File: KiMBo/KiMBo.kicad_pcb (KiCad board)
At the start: 6 copper layers, 187 x 127 mm, 217 parts, among them P1 TOOLHEAD0, P10 ADC, P11 Serial, P12 μUSB, P13 USB_Type_A, P14 μSD, P15 Ethernet, P16 JTAG, P17 LCD, P18 E_MOTOR, P2 TOOLHEAD1, P20 X0_MOTOR, P21 X1_MOTOR, P22 Y_MOTOR, P24 Z0_MOTOR, P27 BED_HEAT, P28 E_HEAT, P29 H_HEAT, P3 DOCK0, P30 DOCK0_HEAT, P31 DOCK1_HEAT, P32 E_FAN, P33 H_FAN, P34 CASE_FAN, P35 PWM, P36 PWR_Input, P4 DOCK1, P5 X1, P6 Y1, P7 Z1, P8 ENC, P9 BED_THERM, U1 OSD3358, U11 74HC595, U12 74HC595, U14 TMC2130, U15 TMC2130, U16 TMC2130, U20 TMC2130, U21 TMC2130, U5 EMMC**G-S100, U6 TPS2051B

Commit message: Complete stepper footprint association, move silkscreen, start DC fuse, polarity protection, and circuit
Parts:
- added C1: 100nF, Capacitors_SMD:C_0603, F.Cu at (409.4, 81.5)
- added C10: 470μF, KiMBo:c_elec_16x16.5, F.Cu at (499.8, 73.6)
- added C11: 220μF, KiMBo:c_elec_8x10.2, F.Cu at (515.2, 86.1)
- added C12: 22μF, Capacitors_SMD:C_0805, F.Cu at (93.5, 154.0)
- added C13: 22μF, Capacitors_SMD:C_0805, F.Cu at (93.5, 156.0)
- added C14: 100nF, Capacitors_SMD:C_0603, F.Cu at (494.3, 151.4)
- added C15: 2.2μF, Capacitors_SMD:C_0805, F.Cu at (469.4, 157.7)
- added C16: 100nF, Capacitors_SMD:C_0603, F.Cu at (488.4, 157.3)
- added C17: 100nF, Capacitors_SMD:C_0603, F.Cu at (484.0, 163.1)
- added C18: 2.2μF, Capacitors_SMD:C_0805, F.Cu at (464.6, 158.6)
- added C187: 100nF, Capacitors_SMD:C_0603, F.Cu at (551.6, 123.4)
- added C188: 4.7nF, Capacitors_SMD:C_0603, F.Cu at (403.4, 131.5)
- added C189: 4.7nF, Capacitors_SMD:C_0603, F.Cu at (410.0, 122.6)
- added C19: 100nF, Capacitors_SMD:C_0603, F.Cu at (477.6, 169.4)
- added C190: 4.7nF, Capacitors_SMD:C_0603, F.Cu at (389.0, 149.8)
- added C191: 4.7nF, Capacitors_SMD:C_0603, F.Cu at (408.0, 130.7)
- added C192: 4.7nF, Capacitors_SMD:C_0603, F.Cu at (402.9, 137.3)
- added C193: 4.7nF, Capacitors_SMD:C_0603, F.Cu at (436.8, 138.1)
- added C194: 4.7nF, Capacitors_SMD:C_0603, F.Cu at (461.5, 116.8)
- added C195: 4.7nF, Capacitors_SMD:C_0603, F.Cu at (447.3, 131.5)
- added C196: 47pF, Capacitors_SMD:C_0603, F.Cu at (515.9, 106.8)
- added C197: 47pF, Capacitors_SMD:C_0603, F.Cu at (498.5, 124.3)
- added C198: 47pF, Capacitors_SMD:C_0603, F.Cu at (510.7, 112.6)
- added C199: 47pF, Capacitors_SMD:C_0603, F.Cu at (502.9, 124.3)
- added C2: 100nF, Capacitors_SMD:C_0603, F.Cu at (402.9, 94.2)
- added C20: 2.2μF, Capacitors_SMD:C_0805, F.Cu at (461.1, 165.2)
- added C200: 47pF, Capacitors_SMD:C_0603, F.Cu at (515.1, 112.6)
- added C201: 47pF, Capacitors_SMD:C_0603, F.Cu at (520.3, 106.8)
- added C202: 47pF, Capacitors_SMD:C_0603, F.Cu at (503.8, 118.5)
- added C203: 47pF, Capacitors_SMD:C_0603, F.Cu at (512.6, 118.5)
- added C204: 47pF, Capacitors_SMD:C_0603, F.Cu at (520.5, 124.3)
- added C205: 47pF, Capacitors_SMD:C_0603, F.Cu at (516.1, 124.3)
- added C206: 47pF, Capacitors_SMD:C_0603, F.Cu at (517.0, 118.5)
- added C207: 47pF, Capacitors_SMD:C_0603, F.Cu at (511.7, 124.3)
- added C208: 47pF, Capacitors_SMD:C_0603, F.Cu at (519.5, 112.6)
- added C209: 47pF, Capacitors_SMD:C_0603, F.Cu at (507.3, 124.3)
- added C21: 4.7μF, Capacitors_SMD:C_0805, F.Cu at (476.1, 151.6)
- added C210: 47pF, Capacitors_SMD:C_0603, F.Cu at (511.5, 106.8)
- added C211: 47pF, Capacitors_SMD:C_0603, F.Cu at (508.2, 118.5)
- added C22: 100nF, Capacitors_SMD:C_0603, F.Cu at (478.8, 163.5)
- added C23: 100nF, Capacitors_SMD:C_0603, F.Cu at (483.2, 157.3)
- added C24: 220μF, Capacitors_Tantalum_SMD:TantalC_SizeD_EIA-7343_Reflow, F.Cu at (559.2, 70.6)
- added C25: 100nF, Capacitors_SMD:C_0603, F.Cu at (571.0, 81.2)
- added C26: 100nF, Capacitors_SMD:C_0603, F.Cu at (566.6, 75.3)
- added C27: 100nF, Capacitors_SMD:C_0603, F.Cu at (576.2, 80.9)
- added C28: 30pF, Capacitors_SMD:C_0603, F.Cu at (466.2, 86.7)
- added C29: 30pF, Capacitors_SMD:C_0603, F.Cu at (480.2, 75.0)
- added C3: 10nF, Capacitors_SMD:C_0603, F.Cu at (402.3, 100.0)
- added C30: 100nF, Capacitors_SMD:C_0603, F.Cu at (464.3, 92.6)
- added C31: 100nF, Capacitors_SMD:C_0603, F.Cu at (474.2, 80.9)
- added C32: 100nF, Capacitors_SMD:C_0603, F.Cu at (470.9, 86.7)
- added C33: 470pF, Capacitors_SMD:C_0603, F.Cu at (450.4, 80.9)
- added C34: 10μF, Capacitors_SMD:C_0805, F.Cu at (436.3, 90.6)
- added C35: 1μF, Capacitors_SMD:C_0603, F.Cu at (481.6, 69.2)
- added C36: DNP-15pF, Capacitors_SMD:C_0603, F.Cu at (429.9, 83.2)
- added C37: DNP-15pF, Capacitors_SMD:C_0603, F.Cu at (429.9, 89.0)
- added C38: DNP-15pF, Capacitors_SMD:C_0603, F.Cu at (443.6, 78.7)
- added C39: DNP-15pF, Capacitors_SMD:C_0603, F.Cu at (452.3, 69.2)
- added C4: 10nF, Capacitors_SMD:C_0603, F.Cu at (407.6, 93.2)
- added C40: 10μF, Capacitors_SMD:C_0603, F.Cu at (536.0, 162.7)
- added C41: 10μF, Capacitors_SMD:C_0603, F.Cu at (540.4, 156.9)
- added C42: 18pF, Capacitors_SMD:C_0603, F.Cu at (524.8, 141.1)
- added C43: 18pF, Capacitors_SMD:C_0603, F.Cu at (520.6, 141.1)
- added C44: 18pF, Capacitors_SMD:C_0603, F.Cu at (529.4, 135.2)
- added C45: 18pF, Capacitors_SMD:C_0603, F.Cu at (525.2, 135.2)
- added C46: 4.7μF, Capacitors_SMD:C_0603, F.Cu at (523.4, 162.7)
- added C47: 4.7μF, Capacitors_SMD:C_0603, F.Cu at (528.2, 162.7)
- added C48: 39nF, Capacitors_SMD:C_0603, F.Cu at (442.1, 161.8)
- added C49: 39nF, Capacitors_SMD:C_0603, F.Cu at (421.1, 181.7)
- added C5: 100nF, Capacitors_SMD:C_0603, F.Cu at (413.0, 87.3)
- added C50: 100nF, Capacitors_SMD:C_0603, F.Cu at (426.1, 175.9)
- added C51: 100nF, Capacitors_SMD:C_0603, F.Cu at (437.4, 167.6)
- added C52: 100nF, Capacitors_SMD:C_0603, F.Cu at (437.4, 161.8)
- added C53: 100nF, Capacitors_SMD:C_0603, F.Cu at (550.8, 110.7)
- added C54: 100nF, Capacitors_SMD:C_0603, F.Cu at (554.2, 104.8)
- added C55: 100nF, Capacitors_SMD:C_0603, F.Cu at (559.1, 99.0)
- added C56: 100nF, Capacitors_SMD:C_0603, F.Cu at (549.1, 104.8)
- added C57: 100nF, Capacitors_SMD:C_0603, F.Cu at (554.0, 99.0)
- added C58: 100nF, Capacitors_SMD:C_0603, F.Cu at (531.0, 108.1)
- added C6: 22nF, Capacitors_SMD:C_0603, F.Cu at (393.1, 93.6)
- added C61: 100nF, Capacitors_SMD:C_0603, F.Cu at (415.5, 191.3)
- added C7: 100nF, Capacitors_SMD:C_0603, F.Cu at (397.7, 93.6)
- added C8: 2.2μF, Capacitors_SMD:C_0603, F.Cu at (376.4, 181.5)
- added C9: 100nF, Capacitors_SMD:C_0603, F.Cu at (381.4, 181.5)
- added D1: D5V0F1U2S9, KiMBo:SOD-923, F.Cu at (379.9, 104.0)
- added D10: TPD1E04U04DPYR, KiMBo:TPD_PX1SON, F.Cu at (350.4, 168.4)
- added D11: LED, LEDs:LED_0603, F.Cu at (356.4, 174.3)
- added D12: DNP-TLVH431, TO_SOT_Packages_SMD:SOT-23, F.Cu at (349.0, 174.2)
- added D13: SK54A-LTP, KiMBo:SK-DO-214AC, F.Cu at (532.1, 70.2)
- added D14: D5V0F1U2S9, KiMBo:SOD-923, F.Cu at (526.0, 82.5)
- added D15: SMAZ10, KiMBo:SMA-DO-214AC, F.Cu at (83.5, 152.0)
- added D16: SMAJ26A, KiMBo:SK-DO-214AC, F.Cu at (92.5, 160.0)
- added D17: TPD1E04U04DPYR, KiMBo:TPD_PX1SON, F.Cu at (410.1, 182.5)
- added D18: SK1545-TP, KiMBo:SK-DO-214AB, F.Cu at (377.3, 133.5)
- added D19: LED, LEDs:LED_0603, F.Cu at (416.2, 133.9)
- added D2: TPD1E04U04DPYR, KiMBo:TPD_PX1SON, F.Cu at (397.9, 82.9)
- added D20: MBRA340T3, KiMBo:MBR-DO-214AC, F.Cu at (402.4, 117.8)
- added D21: MBRA340T3, KiMBo:MBR-DO-214AC, F.Cu at (364.6, 146.1)
- added D22: LED, LEDs:LED_0603, F.Cu at (366.0, 152.8)
- added D23: LED, LEDs:LED_0603, F.Cu at (362.6, 152.8)
- added D24: MBRA340T3, KiMBo:MBR-DO-214AC, F.Cu at (387.0, 124.5)
- added D25: MBRA340T3, KiMBo:MBR-DO-214AC, F.Cu at (357.5, 146.1)
- added D26: LED, LEDs:LED_0603, F.Cu at (359.1, 152.8)
- added D27: LED, LEDs:LED_0603, F.Cu at (355.7, 152.8)
- added D28: MBRA340T3, KiMBo:MBR-DO-214AC, F.Cu at (424.6, 136.9)
- added D29: LED, LEDs:LED_0603, F.Cu at (474.9, 116.4)
- added D3: LED, LEDs:LED_0603, F.Cu at (402.2, 105.5)
- added D30: MBRA340T3, KiMBo:MBR-DO-214AC, F.Cu at (435.1, 130.7)
- added D31: LED, LEDs:LED_0603, F.Cu at (460.7, 139.8)
- added D32: MBRA340T3, KiMBo:MBR-DO-214AC, F.Cu at (445.7, 124.4)
- added D33: LED, LEDs:LED_0603, F.Cu at (469.5, 128.1)
- added D4: LED, LEDs:LED_0603, F.Cu at (410.6, 98.6)
- added D5: LED, LEDs:LED_0603, F.Cu at (420.6, 87.5)
- added D6: LED, LEDs:LED_0603, F.Cu at (406.0, 104.5)
- added D7: D5V0F1U2S9, KiMBo:SOD-923, F.Cu at (396.0, 87.9)
- added D8: D5V0F1U2S9, KiMBo:SOD-923, F.Cu at (411.8, 75.8)
- added D9: TLVH431, TO_SOT_Packages_SMD:SOT-23, F.Cu at (370.5, 181.4)
- added FB1: MPZ1608S102ATA00, KiMBo:Ferrite_Bead_0603, F.Cu at (367.3, 104.8)
- added FB10: MMZ1608A252BTA00, KiMBo:Ferrite_Bead_0603, F.Cu at (399.1, 76.6)
- added FB11: MMZ1608A252BTA00, KiMBo:Ferrite_Bead_0603, F.Cu at (383.2, 83.7)
- added FB12: MMZ1608A252BTA00, KiMBo:Ferrite_Bead_0603, F.Cu at (367.4, 97.8)
- added FB13: MMZ1608A252BTA00, KiMBo:Ferrite_Bead_0603, F.Cu at (399.1, 69.6)
- added FB14: MMZ1608A252BTA00, KiMBo:Ferrite_Bead_0603, F.Cu at (351.6, 104.8)
- added FB15: MMZ1608A252BTA00, KiMBo:Ferrite_Bead_0603, F.Cu at (367.4, 90.7)
- added FB16: MMZ1608A252BTA00, KiMBo:Ferrite_Bead_0603, F.Cu at (383.2, 76.6)
- added FB17: MMZ1608A252BTA00, KiMBo:Ferrite_Bead_0603, F.Cu at (351.6, 97.8)
- added FB18: MMZ1608A252BTA00, KiMBo:Ferrite_Bead_0603, F.Cu at (367.4, 83.7)
- added FB19: MPZ1608S102ATA00, KiMBo:Ferrite_Bead_0603, F.Cu at (383.1, 97.8)
- added FB2: MPZ1608S102ATA00, KiMBo:Ferrite_Bead_0603, F.Cu at (414.8, 69.6)
- added FB20: MMZ1608A252BTA00, KiMBo:Ferrite_Bead_0603, F.Cu at (383.2, 69.6)
- added FB21: MPZ1608S102ATA00, KiMBo:Ferrite_Bead_0603, F.Cu at (351.5, 162.2)
- added FB22: BLM31SN500SN1L, Resistors_SMD:R_1206_HandSoldering, F.Cu at (84.0, 145.0)
- added FB23: BLM31SN500SN1L, Resistors_SMD:R_1206_HandSoldering, F.Cu at (84.0, 148.0)
- added FB24: BLM15AG102SN1D, Resistors_SMD:R_0402, F.Cu at (498.2, 179.1)
- added FB25: BLM15AG102SN1D, Resistors_SMD:R_0402, F.Cu at (498.2, 184.8)
- added FB26: LI0805H151R-10, Resistors_SMD:R_0805, F.Cu at (547.5, 69.4)
- added FB27: LI0805H151R-10, Resistors_SMD:R_0805, F.Cu at (432.5, 77.1)
- added FB28: MMZ1608A252BTA00, KiMBo:Ferrite_Bead_0603, F.Cu at (508.4, 164.3)
- added FB29: MMZ1608A252BTA00, KiMBo:Ferrite_Bead_0603, F.Cu at (508.4, 157.3)
- added FB3: MMZ1608A252BTA00, KiMBo:Ferrite_Bead_0603, F.Cu at (351.6, 90.7)
- added FB30: MMZ1608A252BTA00, KiMBo:Ferrite_Bead_0603, F.Cu at (427.1, 169.2)
- added FB31: MMZ1608A252BTA00, KiMBo:Ferrite_Bead_0603, F.Cu at (411.3, 162.2)
- added FB32: MMZ1608A252BTA00, KiMBo:Ferrite_Bead_0603, F.Cu at (411.3, 176.3)
- added FB33: MMZ1608A252BTA00, KiMBo:Ferrite_Bead_0603, F.Cu at (427.1, 162.2)
- added FB34: MMZ1608A252BTA00, KiMBo:Ferrite_Bead_0603, F.Cu at (411.3, 169.2)
- added FB35: BLM31SN500SN1L, Resistors_SMD:R_1206_HandSoldering, F.Cu at (381.4, 117.2)
- added FB36: BLM31SN500SN1L, Resistors_SMD:R_1206_HandSoldering, F.Cu at (365.9, 125.6)
- added FB37: FBMH4532HM132-T, KiMBo:Ferrite_Bead_1812, F.Cu at (351.2, 134.9)
- added FB38: FBMH4532HM132-T, KiMBo:Ferrite_Bead_1812, F.Cu at (366.6, 118.1)
- added FB39: FBMH4532HM132-T, KiMBo:Ferrite_Bead_1812, F.Cu at (351.2, 126.5)
- added FB4: MMZ1608A252BTA00, KiMBo:Ferrite_Bead_0603, F.Cu at (367.4, 76.6)
- added FB40: FBMH4532HM132-T, KiMBo:Ferrite_Bead_1812, F.Cu at (351.2, 118.1)
- added FB41: CIM21J202NE, Resistors_SMD:R_0805, F.Cu at (426.4, 117.0)
- added FB42: CIM21J202NE, Resistors_SMD:R_0805, F.Cu at (426.4, 123.2)
- added FB43: CIM21J202NE, Resistors_SMD:R_0805, F.Cu at (437.0, 117.0)
- added FB5: MMZ1608A252BTA00, KiMBo:Ferrite_Bead_0603, F.Cu at (351.6, 83.7)
- added FB6: MMZ1608A252BTA00, KiMBo:Ferrite_Bead_0603, F.Cu at (367.4, 69.6)
- added FB7: MMZ1608A252BTA00, KiMBo:Ferrite_Bead_0603, F.Cu at (351.6, 76.6)
- added FB8: MMZ1608A252BTA00, KiMBo:Ferrite_Bead_0603, F.Cu at (351.6, 69.6)
- added FB9: MMZ1608A252BTA00, KiMBo:Ferrite_Bead_0603, F.Cu at (383.2, 90.7)
- added IC1: 24LC32AT-I/OT, TO_SOT_Packages_SMD:SOT-23-5, F.Cu at (459.4, 152.1)
- added L1: 47μH, KiMBo:IHLP_Inductor, F.Cu at (496.3, 85.9)
- added OSC1: ASDMB, KiMBo:Crystal_SMD_ASDMB_4Pads, F.Cu at (456.0, 166.1)
- added Q1: 2N7002, TO_SOT_Packages_SMD:SOT-23, F.Cu at (388.1, 104.8)
- added Q10: DMP3098L-7, TO_SOT_Packages_SMD:SOT-23, F.Cu at (348.7, 142.3)
- added Q11: 2N7002, TO_SOT_Packages_SMD:SOT-23, F.Cu at (371.3, 145.5)
- added Q12: 2N7002, TO_SOT_Packages_SMD:SOT-23, F.Cu at (400.0, 125.2)
- added Q13: DMP3098L-7, TO_SOT_Packages_SMD:SOT-23, F.Cu at (393.6, 117.1)
- added Q14: DMP3098L-7, TO_SOT_Packages_SMD:SOT-23, F.Cu at (378.2, 125.5)
- added Q15: 2N7002, TO_SOT_Packages_SMD:SOT-23, F.Cu at (441.8, 131.8)
- added Q16: DMP3098L-7, TO_SOT_Packages_SMD:SOT-23, F.Cu at (437.0, 123.4)
- added Q17: 2N7002, TO_SOT_Packages_SMD:SOT-23, F.Cu at (456.0, 117.1)
- added Q18: DMP3098L-7, TO_SOT_Packages_SMD:SOT-23, F.Cu at (447.6, 117.1)
- added Q19: 2N7002, TO_SOT_Packages_SMD:SOT-23, F.Cu at (431.3, 138.1)
- added Q2: MMBT2907, TO_SOT_Packages_SMD:SOT-23, F.Cu at (371.7, 168.7)
- added Q20: DMP3098L-7, TO_SOT_Packages_SMD:SOT-23, F.Cu at (426.3, 129.6)
- added Q3: DNP-MMBT2907, TO_SOT_Packages_SMD:SOT-23, F.Cu at (365.4, 162.1)
- added Q4: IPD90P03P4-04, TO_SOT_Packages_SMD:TO-252-2Lead, F.Cu at (78.5, 158.0)
- added Q5: 2N7002, TO_SOT_Packages_SMD:SOT-23, F.Cu at (393.0, 131.9)
- added Q6: IPD90P03P4-04, TO_SOT_Packages_SMD:TO-252-2Lead, F.Cu at (365.4, 140.3)
- added Q7: 2N7002, TO_SOT_Packages_SMD:SOT-23, F.Cu at (386.6, 131.9)
- added Q8: 2N7002, TO_SOT_Packages_SMD:SOT-23, F.Cu at (393.7, 123.7)
- added Q9: DMP3098L-7, TO_SOT_Packages_SMD:SOT-23, F.Cu at (348.7, 148.9)
- added R1: 1kΩ, Resistors_SMD:R_0603, F.Cu at (417.3, 87.9)
- added R10: 4.75kΩ, Resistors_SMD:R_0603, F.Cu at (394.2, 99.4)
- added R100: 100Ω, Resistors_SMD:R_0603, F.Cu at (430.3, 181.7)
- added R101: 4.7kΩ, Resistors_SMD:R_0603, F.Cu at (437.2, 173.5)
- added R102: 4.7kΩ, Resistors_SMD:R_0603, F.Cu at (446.6, 161.8)
- added R103: 4.7kΩ, Resistors_SMD:R_0603, F.Cu at (442.4, 167.6)
- added R104: 4.7kΩ, Resistors_SMD:R_0603, F.Cu at (544.1, 99.0)
- added R105: 4.7kΩ, Resistors_SMD:R_0603, F.Cu at (539.2, 104.8)
- added R106: 4.7kΩ, Resistors_SMD:R_0603, F.Cu at (548.9, 99.0)
- added R107: 4.7kΩ, Resistors_SMD:R_0603, F.Cu at (536.0, 110.7)
- added R108: 4.7kΩ, Resistors_SMD:R_0603, F.Cu at (544.1, 104.8)
- added R109: 4.7kΩ, Resistors_SMD:R_0603, F.Cu at (530.8, 114.0)
- added R11: 4.75kΩ, Resistors_SMD:R_0603, F.Cu at (394.2, 105.3)
- added R110: 4.7kΩ, Resistors_SMD:R_0603, F.Cu at (539.2, 99.0)
- added R111: 4.7kΩ, Resistors_SMD:R_0603, F.Cu at (540.9, 110.7)
- added R112: 4.7kΩ, Resistors_SMD:R_0603, F.Cu at (555.8, 110.7)
- added R113: 4.7kΩ, Resistors_SMD:R_0603, F.Cu at (559.3, 104.8)
- added R114: 4.7kΩ, Resistors_SMD:R_0603, F.Cu at (545.7, 110.7)
- added R115: 4.7kΩ, Resistors_SMD:R_0603, F.Cu at (405.6, 191.3)
- added R116: 4.7kΩ, Resistors_SMD:R_0603, F.Cu at (410.5, 191.3)
- added R12: 4.7kΩ, Resistors_SMD:R_0603, F.Cu at (408.0, 87.3)
- added R122: 4.7kΩ, Resistors_SMD:R_0603, F.Cu at (482.6, 135.2)
- added R123: 4.7kΩ, Resistors_SMD:R_0603, F.Cu at (487.5, 135.2)
- added R124: 4.7kΩ, Resistors_SMD:R_0603, F.Cu at (492.4, 135.2)
- added R13: 4.7kΩ, Resistors_SMD:R_0603, F.Cu at (419.2, 76.2)
- added R130: 4.7kΩ, Resistors_SMD:R_0603, F.Cu at (433.7, 191.3)
- added R131: 4.7kΩ, Resistors_SMD:R_0603, F.Cu at (428.8, 191.3)
- added R132: 4.7kΩ, Resistors_SMD:R_0603, F.Cu at (423.9, 191.3)
- added R138: 4.7kΩ, Resistors_SMD:R_0603, F.Cu at (442.4, 106.8)
- added R14: 10kΩ, Resistors_SMD:R_0603, F.Cu at (376.2, 175.6)
- added R144: 4.7kΩ, Resistors_SMD:R_0603, F.Cu at (456.1, 106.8)
- added R15: 10kΩ, Resistors_SMD:R_0603, F.Cu at (388.8, 167.8)
- added R150: 4.7kΩ, Resistors_SMD:R_0603, F.Cu at (428.1, 106.8)
- added R151: 4.7kΩ, Resistors_SMD:R_0603, F.Cu at (432.9, 106.8)
- added R157: 4.7kΩ, Resistors_SMD:R_0603, F.Cu at (568.2, 123.4)
- added R158: 4.7kΩ, Resistors_SMD:R_0603, F.Cu at (573.1, 123.4)
- added R159: 4.7kΩ, Resistors_SMD:R_0603, F.Cu at (578.0, 123.4)
- added R16: 499Ω, Resistors_SMD:R_0603, F.Cu at (371.6, 175.0)
- added R165: 4.7kΩ, Resistors_SMD:R_0603, F.Cu at (423.5, 151.4)
- added R17: DNPΩ, Resistors_SMD:R_0603, F.Cu at (395.6, 161.8)
- added R171: 4.7kΩ, Resistors_SMD:R_0603, F.Cu at (546.6, 123.4)
- added R172: 10Ω, Resistors_SMD:R_0603, F.Cu at (388.8, 138.1)
- added R173: 4.7kΩ, Resistors_SMD:R_0603, F.Cu at (376.9, 146.9)
- added R174: 4.7kΩ, Resistors_SMD:R_0603, F.Cu at (370.6, 151.7)
- added R175: 4.7kΩ, Resistors_SMD:R_0603, F.Cu at (376.9, 141.1)
- added R176: 10kΩ, Resistors_SMD:R_0603, F.Cu at (414.3, 148.3)
- added R177: 10kΩ, Resistors_SMD:R_0603, F.Cu at (384.5, 149.8)
- added R178: 10Ω, Resistors_SMD:R_0603, F.Cu at (409.9, 149.0)
- added R179: 10Ω, Resistors_SMD:R_0603, F.Cu at (412.3, 142.4)
- added R18: 10kΩ, Resistors_SMD:R_0603, F.Cu at (391.0, 161.8)
- added R180: 4.7kΩ, Resistors_SMD:R_0603, F.Cu at (405.2, 149.0)
- added R181: 4.7kΩ, Resistors_SMD:R_0603, F.Cu at (400.4, 149.0)
- added R182: 4.7kΩ, Resistors_SMD:R_0603, F.Cu at (408.4, 116.8)
- added R183: 4.7kΩ, Resistors_SMD:R_0603, F.Cu at (407.1, 143.2)
- added R184: 4.7kΩ, Resistors_SMD:R_0603, F.Cu at (402.2, 143.2)
- added R185: 4.7kΩ, Resistors_SMD:R_0603, F.Cu at (407.7, 137.3)
- added R186: 10kΩ, Resistors_SMD:R_0603, F.Cu at (412.6, 128.5)
- added R187: 10kΩ, Resistors_SMD:R_0603, F.Cu at (397.6, 143.2)
- added R188: 10kΩ, Resistors_SMD:R_0603, F.Cu at (412.3, 136.6)
- added R189: 10kΩ, Resistors_SMD:R_0603, F.Cu at (380.1, 152.8)
- added R19: 40.2kΩ, Resistors_SMD:R_0603, F.Cu at (381.3, 175.6)
- added R190: 10Ω, Resistors_SMD:R_0603, F.Cu at (393.2, 138.1)
- added R191: 10Ω, Resistors_SMD:R_0603, F.Cu at (414.5, 122.6)
- added R192: 4.7kΩ, Resistors_SMD:R_0603, F.Cu at (395.5, 149.0)
- added R193: 4.7kΩ, Resistors_SMD:R_0603, F.Cu at (398.6, 131.5)
- added R194: 4.7kΩ, Resistors_SMD:R_0603, F.Cu at (381.8, 144.0)
- added R195: 4.7kΩ, Resistors_SMD:R_0603, F.Cu at (375.4, 152.8)
- added R196: 4.7kΩ, Resistors_SMD:R_0603, F.Cu at (413.3, 116.8)
- added R197: 4.7kΩ, Resistors_SMD:R_0603, F.Cu at (384.2, 138.1)
- added R198: 10kΩ, Resistors_SMD:R_0603, F.Cu at (405.4, 124.9)
- added R199: 10kΩ, Resistors_SMD:R_0603, F.Cu at (386.4, 144.0)
- added R2: 1kΩ, Resistors_SMD:R_0603, F.Cu at (407.2, 99.0)
- added R20: 4.75kΩ, Resistors_SMD:R_0603, F.Cu at (370.0, 187.6)
- added R200: 10kΩ, Resistors_SMD:R_0603, F.Cu at (398.3, 137.3)
- added R201: 10kΩ, Resistors_SMD:R_0603, F.Cu at (390.8, 144.0)
- added R202: 10Ω, Resistors_SMD:R_0603, F.Cu at (471.2, 122.6)
- added R203: 4.7kΩ, Resistors_SMD:R_0603, F.Cu at (451.7, 123.4)
- added R204: 4.7kΩ, Resistors_SMD:R_0603, F.Cu at (466.3, 116.8)
- added R205: 4.7kΩ, Resistors_SMD:R_0603, F.Cu at (456.5, 129.2)
- added R206: 10kΩ, Resistors_SMD:R_0603, F.Cu at (461.2, 128.5)
- added R207: 10kΩ, Resistors_SMD:R_0603, F.Cu at (471.0, 116.8)
- added R208: 10Ω, Resistors_SMD:R_0603, F.Cu at (451.9, 135.1)
- added R209: 4.7kΩ, Resistors_SMD:R_0603, F.Cu at (466.5, 122.6)
- added R21: DNP-499Ω, Resistors_SMD:R_0603, F.Cu at (376.2, 161.8)
- added R210: 4.7kΩ, Resistors_SMD:R_0603, F.Cu at (446.0, 138.1)
- added R211: 4.7kΩ, Resistors_SMD:R_0603, F.Cu at (461.4, 134.3)
- added R212: 10kΩ, Resistors_SMD:R_0603, F.Cu at (451.9, 129.2)
- added R213: 10kΩ, Resistors_SMD:R_0603, F.Cu at (465.6, 128.5)
- added R214: 10Ω, Resistors_SMD:R_0603, F.Cu at (450.7, 140.9)
- added R215: 4.7kΩ, Resistors_SMD:R_0603, F.Cu at (455.3, 140.9)
- added R216: 4.7kΩ, Resistors_SMD:R_0603, F.Cu at (456.5, 135.1)
- added R217: 4.7kΩ, Resistors_SMD:R_0603, F.Cu at (461.6, 122.6)
- added R218: 10kΩ, Resistors_SMD:R_0603, F.Cu at (456.4, 123.4)
- added R219: 10kΩ, Resistors_SMD:R_0603, F.Cu at (441.4, 138.1)
- added R22: DNPΩ, Resistors_SMD:R_0603, F.Cu at (384.2, 167.8)
- added R220: 100Ω, Resistors_SMD:R_0603, F.Cu at (500.9, 112.6)
- added R221: 100kΩ, Resistors_SMD:R_0603, F.Cu at (482.9, 114.6)
- added R222: 100kΩ, Resistors_SMD:R_0603, F.Cu at (482.9, 120.4)
- added R223: 100kΩ, Resistors_SMD:R_0603, F.Cu at (495.9, 106.8)
- added R224: 100kΩ, Resistors_SMD:R_0603, F.Cu at (490.6, 112.6)
- added R225: 100kΩ, Resistors_SMD:R_0603, F.Cu at (482.9, 126.3)
- added R226: 100kΩ, Resistors_SMD:R_0603, F.Cu at (495.9, 112.6)
- added R227: 100kΩ, Resistors_SMD:R_0603, F.Cu at (488.2, 118.5)
- added R228: 100kΩ, Resistors_SMD:R_0603, F.Cu at (501.3, 106.8)
- added R229: 100kΩ, Resistors_SMD:R_0603, F.Cu at (490.6, 106.8)
- added R23: DNP-10kΩ, Resistors_SMD:R_0603, F.Cu at (356.8, 180.5)
- added R230: 100kΩ, Resistors_SMD:R_0603, F.Cu at (506.6, 106.8)
- added R231: 100kΩ, Resistors_SMD:R_0603, F.Cu at (521.9, 118.5)
- added R232: 100kΩ, Resistors_SMD:R_0603, F.Cu at (493.6, 118.5)
- added R233: 100kΩ, Resistors_SMD:R_0603, F.Cu at (488.2, 124.3)
- added R234: 100kΩ, Resistors_SMD:R_0603, F.Cu at (505.8, 112.6)
- added R235: 100kΩ, Resistors_SMD:R_0603, F.Cu at (493.6, 124.3)
- added R236: 100kΩ, Resistors_SMD:R_0603, F.Cu at (498.9, 118.5)
- added R24: DNP-40.2kΩ, Resistors_SMD:R_0603, F.Cu at (362.4, 168.8)
- added R25: 100kΩ, Resistors_SMD:R_0603, F.Cu at (78.5, 152.0)
- added R26: 4.75kΩ, Resistors_SMD:R_0603, F.Cu at (511.6, 179.2)
- added R27: 4.75kΩ, Resistors_SMD:R_0603, F.Cu at (508.1, 185.1)
- added R28: 0Ω, Resistors_SMD:R_0603, F.Cu at (506.9, 179.2)
- added R29: 0Ω, Resistors_SMD:R_0603, F.Cu at (516.2, 179.2)
- added R3: 1kΩ, Resistors_SMD:R_0603, F.Cu at (398.9, 105.9)
- added R30: 0Ω, Resistors_SMD:R_0603, F.Cu at (512.8, 185.1)
- added R31: 0Ω, Resistors_SMD:R_0603, F.Cu at (492.7, 157.3)
- added R32: 0Ω, Resistors_SMD:R_0603, F.Cu at (469.7, 169.6)
- added R33: 33Ω, Resistors_SMD:R_0603, F.Cu at (473.2, 169.4)
- added R34: 10kΩ, Resistors_SMD:R_0603, F.Cu at (488.0, 169.0)
- added R35: 10kΩ, Resistors_SMD:R_0603, F.Cu at (485.1, 151.4)
- added R36: 10kΩ, Resistors_SMD:R_0603, F.Cu at (480.7, 151.4)
- added R37: 10kΩ, Resistors_SMD:R_0603, F.Cu at (469.2, 163.7)
- added R38: 10kΩ, Resistors_SMD:R_0603, F.Cu at (474.0, 163.5)
- added R39: 10kΩ, Resistors_SMD:R_0603, F.Cu at (478.4, 157.7)
- added R4: 1kΩ, Resistors_SMD:R_0603, F.Cu at (417.3, 93.8)
- added R40: 10kΩ, Resistors_SMD:R_0603, F.Cu at (465.7, 169.6)
- added R41: 10kΩ, Resistors_SMD:R_0603, F.Cu at (474.0, 157.7)
- added R42: 10kΩ, Resistors_SMD:R_0603, F.Cu at (489.5, 151.4)
- added R43: 10kΩ, Resistors_SMD:R_0603, F.Cu at (483.6, 169.0)
- added R44: 10kΩ, Resistors_SMD:R_0603, F.Cu at (488.8, 163.1)
- added R45: 10kΩ, Resistors_SMD:R_0603, F.Cu at (493.2, 163.1)
- added R46: 0Ω, Resistors_SMD:R_0603, F.Cu at (574.4, 75.0)
- added R47: 1.5kΩ, Resistors_SMD:R_0603, F.Cu at (557.2, 84.3)
- added R48: 10kΩ, Resistors_SMD:R_0603, F.Cu at (560.9, 78.1)
- added R49: 1.5kΩ, Resistors_SMD:R_0603, F.Cu at (574.5, 69.2)
- added R5: 470Ω, Resistors_SMD:R_0603, F.Cu at (403.2, 88.3)
- added R50: 0Ω, Resistors_SMD:R_0603, F.Cu at (570.9, 75.3)
- added R51: 100mΩ, Resistors_SMD:R_0603, F.Cu at (551.8, 84.3)
- added R52: 0Ω, Resistors_SMD:R_0603, F.Cu at (561.3, 84.0)
- added R53: 100kΩ, Resistors_SMD:R_0603, F.Cu at (565.8, 81.2)
- added R54: 10Ω, Resistors_SMD:R_0603, F.Cu at (453.2, 86.7)
- added R55: DNP-1MΩ, Resistors_SMD:R_0603, F.Cu at (429.7, 94.9)
- added R56: DNP-10Ω, Resistors_SMD:R_0603, F.Cu at (438.1, 84.6)
- added R57: 100Ω, Resistors_SMD:R_0603, F.Cu at (450.5, 92.6)
- added R58: 100Ω, Resistors_SMD:R_0603, F.Cu at (473.1, 69.2)
- added R59: 100Ω, Resistors_SMD:R_0603, F.Cu at (457.3, 86.7)
- added R6: 4.75kΩ, Resistors_SMD:R_0603, F.Cu at (412.7, 93.2)
- added R60: 100Ω, Resistors_SMD:R_0603, F.Cu at (464.8, 80.9)
- added R61: 100Ω, Resistors_SMD:R_0603, F.Cu at (477.6, 69.2)
- added R62: 100Ω, Resistors_SMD:R_0603, F.Cu at (472.3, 75.0)
- added R63: 100Ω, Resistors_SMD:R_0603, F.Cu at (461.8, 86.7)
- added R64: 100Ω, Resistors_SMD:R_0603, F.Cu at (455.1, 92.6)
- added R65: 100Ω, Resistors_SMD:R_0603, F.Cu at (460.3, 80.9)
- added R66: 100Ω, Resistors_SMD:R_0603, F.Cu at (469.4, 80.9)
- added R67: 0Ω, Resistors_SMD:R_0603, F.Cu at (476.3, 75.0)
- added R68: DNP-0Ω, Resistors_SMD:R_0603, F.Cu at (451.5, 75.0)
- added R69: 1.5kΩ, Resistors_SMD:R_0603, F.Cu at (445.8, 92.6)
- added R7: 10kΩ, Resistors_SMD:R_0603, F.Cu at (414.1, 81.5)
- added R70: 49.9Ω, Resistors_SMD:R_0603, F.Cu at (444.5, 84.6)
- added R71: 12.1kΩ, Resistors_SMD:R_0603, F.Cu at (467.1, 75.0)
- added R72: 10kΩ, Resistors_SMD:R_0603, F.Cu at (459.5, 92.6)
- added R73: 49.9Ω, Resistors_SMD:R_0603, F.Cu at (440.6, 96.7)
- added R74: 10kΩ, Resistors_SMD:R_0603, F.Cu at (468.6, 69.2)
- added R75: 49.9Ω, Resistors_SMD:R_0603, F.Cu at (455.5, 80.9)
- added R76: 10kΩ, Resistors_SMD:R_0603, F.Cu at (449.2, 86.7)
- added R77: 49.9Ω, Resistors_SMD:R_0603, F.Cu at (463.9, 69.2)
- added R78: 10kΩ, Resistors_SMD:R_0603, F.Cu at (462.0, 75.0)
- added R79: 10kΩ, Resistors_SMD:R_0603, F.Cu at (435.9, 96.7)
- added R8: 470Ω, Resistors_SMD:R_0603, F.Cu at (418.6, 82.1)
- added R80: 1.5kΩ, Resistors_SMD:R_0603, F.Cu at (440.9, 90.4)
- added R81: 1.5kΩ, Resistors_SMD:R_0603, F.Cu at (457.4, 75.0)
- added R82: 1.5kΩ, Resistors_SMD:R_0603, F.Cu at (458.9, 69.2)
- added R83: 10kΩ, Resistors_SMD:R_0603, F.Cu at (536.0, 156.9)
- added R84: 10kΩ, Resistors_SMD:R_0603, F.Cu at (549.2, 162.7)
- added R85: 10kΩ, Resistors_SMD:R_0603, F.Cu at (553.6, 156.9)
- added R86: 10kΩ, Resistors_SMD:R_0603, F.Cu at (549.2, 156.9)
- added R87: 10kΩ, Resistors_SMD:R_0603, F.Cu at (544.8, 162.7)
- added R88: 10kΩ, Resistors_SMD:R_0603, F.Cu at (540.4, 162.7)
- added R89: 10kΩ, Resistors_SMD:R_0603, F.Cu at (544.8, 156.9)
- added R9: 0Ω, Resistors_SMD:R_0603, F.Cu at (398.7, 99.4)
- added R90: DNP-1MΩ, Resistors_SMD:R_0603, F.Cu at (519.0, 135.2)
- added R91: 1MΩ, Resistors_SMD:R_0603, F.Cu at (516.6, 143.0)
- added R92: 4.7kΩ, Resistors_SMD:R_0603, F.Cu at (527.3, 156.9)
- added R93: 10kΩ, Resistors_SMD:R_0603, F.Cu at (522.7, 156.9)
- added R94: 4.7kΩ, Resistors_SMD:R_0603, F.Cu at (518.5, 162.7)
- added R95: 10kΩ, Resistors_SMD:R_0603, F.Cu at (518.3, 156.9)
- added R96: 100Ω, Resistors_SMD:R_0603, F.Cu at (421.2, 175.9)
- added R97: 4.7kΩ, Resistors_SMD:R_0603, F.Cu at (425.6, 181.7)
- added R98: 100Ω, Resistors_SMD:R_0603, F.Cu at (431.0, 175.9)
- added R99: 4.7kΩ, Resistors_SMD:R_0603, F.Cu at (435.7, 179.3)
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- renumbered C59 to C107, C60 to C108, C61 to C109, C62 to C110, C63 to C111, C64 to C112, C65 to C113, C66 to C114, C67 to C115, C68 to C116, C69 to C117, C70 to C118, C71 to C119, C72 to C120, C73 to C121, C74 to C122, C59 to C123, C60 to C124, C61 to C125, C62 to C126, C63 to C127, C64 to C128, C65 to C129, C66 to C130, C67 to C131, C68 to C132, C69 to C133, C70 to C134, C71 to C135, C72 to C136, C73 to C137, C74 to C138, C59 to C139, C60 to C140, C61 to C141, C62 to C142, C63 to C143, C64 to C144, C65 to C145, C66 to C146, C67 to C147, C68 to C148, C69 to C149, C70 to C150, C71 to C151, C72 to C152, C73 to C153, C74 to C154, R117 to R139, R118 to R140, R119 to R141, R120 to R142, R121 to R143, R117 to R145, R118 to R146, R119 to R147, R120 to R148, R121 to R149, R117 to R152, R118 to R153, R119 to R154, R120 to R155, R121 to R156, U14 to U17, U14 to U18, U14 to U19
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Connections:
- C108 pad 1: Net-(C60-Pad1) -> Net-(C108-Pad1)
- C110 pad 1: /Stepper Drivers/E Stepper Driver/5VOUT -> /Stepper Drivers/Z1 Stepper Driver/5VOUT
- C111 pad 1: Net-(C63-Pad1) -> Net-(C111-Pad1)
- C111 pad 2: Net-(C63-Pad2) -> Net-(C111-Pad2)
- C112 pad 1: /Stepper Drivers/E_A2 -> /Stepper Drivers/Z1_A2
- C113 pad 1: /Stepper Drivers/E_B2 -> /Stepper Drivers/Z1_B2
- C114 pad 2: Net-(C66-Pad2) -> Net-(C114-Pad2)
- C115 pad 1: /Stepper Drivers/E_A1 -> /Stepper Drivers/Z1_A1
- C116 pad 1: /Stepper Drivers/E_B1 -> /Stepper Drivers/Z1_B1
- C119 pad 1: Net-(C71-Pad1) -> Net-(C119-Pad1)
- C122 pad 1: Net-(C74-Pad1) -> Net-(C122-Pad1)
- C124 pad 1: Net-(C60-Pad1) -> Net-(C124-Pad1)
- C126 pad 1: /Stepper Drivers/E Stepper Driver/5VOUT -> /Stepper Drivers/Z2 Stepper Driver/5VOUT
- C127 pad 1: Net-(C63-Pad1) -> Net-(C127-Pad1)
- C127 pad 2: Net-(C63-Pad2) -> Net-(C127-Pad2)
- C128 pad 1: /Stepper Drivers/E_A2 -> /Stepper Drivers/Z2_A2
- C129 pad 1: /Stepper Drivers/E_B2 -> /Stepper Drivers/Z2_B2
- C130 pad 2: Net-(C66-Pad2) -> Net-(C130-Pad2)
- C131 pad 1: /Stepper Drivers/E_A1 -> /Stepper Drivers/Z2_A1
- C132 pad 1: /Stepper Drivers/E_B1 -> /Stepper Drivers/Z2_B1
- C135 pad 1: Net-(C71-Pad1) -> Net-(C135-Pad1)
- C138 pad 1: Net-(C74-Pad1) -> Net-(C138-Pad1)
- C140 pad 1: Net-(C60-Pad1) -> Net-(C140-Pad1)
- C142 pad 1: /Stepper Drivers/E Stepper Driver/5VOUT -> /Stepper Drivers/H Stepper Driver/5VOUT
- C143 pad 1: Net-(C63-Pad1) -> Net-(C143-Pad1)
- C143 pad 2: Net-(C63-Pad2) -> Net-(C143-Pad2)
- C144 pad 1: /Stepper Drivers/E_A2 -> /Stepper Drivers/H_A2
- C145 pad 1: /Stepper Drivers/E_B2 -> /Stepper Drivers/H_B2
- C146 pad 2: Net-(C66-Pad2) -> Net-(C146-Pad2)
- C147 pad 1: /Stepper Drivers/E_A1 -> /Stepper Drivers/H_A1
- C148 pad 1: /Stepper Drivers/E_B1 -> /Stepper Drivers/H_B1
- C151 pad 1: Net-(C71-Pad1) -> Net-(C151-Pad1)
- C154 pad 1: Net-(C74-Pad1) -> Net-(C154-Pad1)
- P19 pad 1: /Stepper Drivers/E_A2 -> /Stepper Drivers/H_A2
- P19 pad 2: /Stepper Drivers/E_A1 -> /Stepper Drivers/H_A1
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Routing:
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- added copper zone on F.Cu, net /Stepper Drivers/H_A1
- added copper zone on In2.Cu, net /Stepper Drivers/H_A1
- added copper zone on F.Cu, net /Stepper Drivers/H_A2
- added copper zone on In2.Cu, net /Stepper Drivers/H_A2
- added copper zone on F.Cu, net /Stepper Drivers/H_B1
- added copper zone on In2.Cu, net /Stepper Drivers/H_B1
- added copper zone on F.Cu, net /Stepper Drivers/H_B2
- added copper zone on In2.Cu, net /Stepper Drivers/H_B2
- added copper zone on F.Cu, net /Stepper Drivers/Z1_A1
- added copper zone on In2.Cu, net /Stepper Drivers/Z1_A1
- added copper zone on F.Cu, net /Stepper Drivers/Z1_A2
- added copper zone on In2.Cu, net /Stepper Drivers/Z1_A2
- added copper zone on F.Cu, net /Stepper Drivers/Z1_B1
- added copper zone on In2.Cu, net /Stepper Drivers/Z1_B1
- added copper zone on F.Cu, net /Stepper Drivers/Z1_B2
- added copper zone on In2.Cu, net /Stepper Drivers/Z1_B2
- added copper zone on F.Cu, net /Stepper Drivers/Z2_A1
- added copper zone on In2.Cu, net /Stepper Drivers/Z2_A1
- added copper zone on F.Cu, net /Stepper Drivers/Z2_A2
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
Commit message: Begin laying out the bed heater circuit
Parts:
- added REF**: MountingHole_3mm_Pad, KiMBo:MountingHole_3mm_Pad, F.Cu at (66.0, 164.0)
- moved C188 329.4 mm to (74.0, 125.2), turned to 180 degrees
- moved R177 312.9 mm to (72.0, 133.5), turned to 270 degrees
- moved FB35 307.7 mm to (74.0, 130.5), turned to 180 degrees
- moved Q5 298.5 mm to (94.5, 127.8), turned to 180 degrees
- moved FB36 291.9 mm to (74.0, 127.5), turned to 180 degrees
- moved R172 291.3 mm to (97.8, 126.8)
- moved D18 290.3 mm to (87.0, 136.0)
- moved D19 288.7 mm to (134.2, 71.9)
- moved R176 288.7 mm to (132.3, 86.3)
- moved R175 283.4 mm to (93.8, 130.5)
- moved R174 280.2 mm to (91.2, 129.8), turned to 270 degrees
- moved R173 279.8 mm to (97.8, 128.5)
- moved Q6 277.6 mm to (88.0, 129.0), turned to 90 degrees
- moved U3 27.6 mm to (118.3, 121.0)
- moved D16 18.6 mm to (78.8, 147.4), turned to 270 degrees
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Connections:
- net /PWM/BED_HEAT renamed /Heaters/BED_HEAT_IN
- net /PWM/CASE_FAN renamed /Fans/CASE_FAN_IN
- net /PWM/DOCK0_HEAT renamed /Heaters/DOCK0_HEAT_IN
- net /PWM/DOCK1_HEAT renamed /Heaters/DOCK1_HEAT_IN
- net /PWM/E_FAN renamed /Fans/E_FAN_IN
- net /PWM/E_HEAT renamed /Heaters/E_HEAT_IN
- net /PWM/H_FAN renamed /Fans/H_FAN_IN
- net /PWM/H_HEAT renamed /Heaters/H_HEAT_IN
- Q10 pad 2: +24V -> Net-(D21-Pad1)
- Q10 pad 3: Net-(D21-Pad1) -> +24V
- Q13 pad 2: +24V -> Net-(D24-Pad1)
- Q13 pad 3: Net-(D24-Pad1) -> +24V
- Q14 pad 2: +24V -> Net-(D25-Pad1)
- Q14 pad 3: Net-(D25-Pad1) -> +24V
- Q16 pad 2: +24V -> Net-(D28-Pad1)
- Q16 pad 3: Net-(D28-Pad1) -> +24V
- Q18 pad 2: +24V -> Net-(D30-Pad1)
- Q18 pad 3: Net-(D30-Pad1) -> +24V
- Q20 pad 2: +24V -> Net-(D32-Pad1)
- Q20 pad 3: Net-(D32-Pad1) -> +24V
- Q4 pad 2: Net-(D15-Pad1) -> Net-(F1-Pad2)
- Q4 pad 3: Net-(F1-Pad2) -> Net-(D15-Pad1)
- Q6 pad 2: +24V -> Net-(D18-Pad1)
- Q6 pad 3: Net-(D18-Pad1) -> +24V
- Q9 pad 2: +24V -> Net-(D20-Pad1)
- Q9 pad 3: Net-(D20-Pad1) -> +24V
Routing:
- net /SPI1_SCLK: track 26.4 -> 189.5 mm
- net +24V: track 255.4 -> 343.6 mm, vias 88 -> 157
- net (no net): track 0.00 -> 38.5 mm, vias 0 -> 1
- net Net-(D15-Pad1): track 0.00 -> 36.5 mm, vias 0 -> 30
- net Net-(F1-Pad2): track 0.00 -> 20.0 mm, vias 0 -> 13
- net Net-(D18-Pad1): track 0.00 -> 20.0 mm, vias 0 -> 15
- net CGND: track 892.8 -> 903.6 mm
- net Net-(D15-Pad2): track 0.00 -> 7.37 mm
- net Net-(Q6-Pad1): track 0.00 -> 5.33 mm
- net Net-(Q5-Pad3): track 0.00 -> 1.75 mm
- net /Heaters/BED_HEAT_IN: track 0.00 -> 1.75 mm
- net Net-(Q5-Pad1): track 0.00 -> 1.55 mm
- net /Heaters/BED_HEAT: vias 0 -> 2
- added copper zone on B.Cu, net +24V
- added copper zone on In2.Cu, net +24V
- added copper zone on In3.Cu, net +24V
- added copper zone on B.Cu, net /Heaters/BED_HEAT
- added copper zone on F.Cu, net /Heaters/BED_HEAT
- added copper zone on In2.Cu, net /Heaters/BED_HEAT
- added copper zone on In3.Cu, net /Heaters/BED_HEAT
- added copper zone on In4.Cu, net /Heaters/BED_HEAT
- added copper zone on B.Cu, net Net-(D15-Pad1)
- added copper zone on F.Cu, net Net-(D15-Pad1)
- added copper zone on In2.Cu, net Net-(D15-Pad1)
- added copper zone on In3.Cu, net Net-(D15-Pad1)
- added copper zone on In4.Cu, net Net-(D15-Pad1)
- added copper zone on B.Cu, net Net-(D18-Pad1)
- added copper zone on F.Cu, net Net-(D18-Pad1)
- added copper zone on In2.Cu, net Net-(D18-Pad1)
- added copper zone on In3.Cu, net Net-(D18-Pad1)
- added copper zone on In4.Cu, net Net-(D18-Pad1)
- added copper zone on B.Cu, net Net-(F1-Pad2)
- added copper zone on In2.Cu, net Net-(F1-Pad2)
- added copper zone on In3.Cu, net Net-(F1-Pad2)
- added copper zone on In4.Cu, net Net-(F1-Pad2)

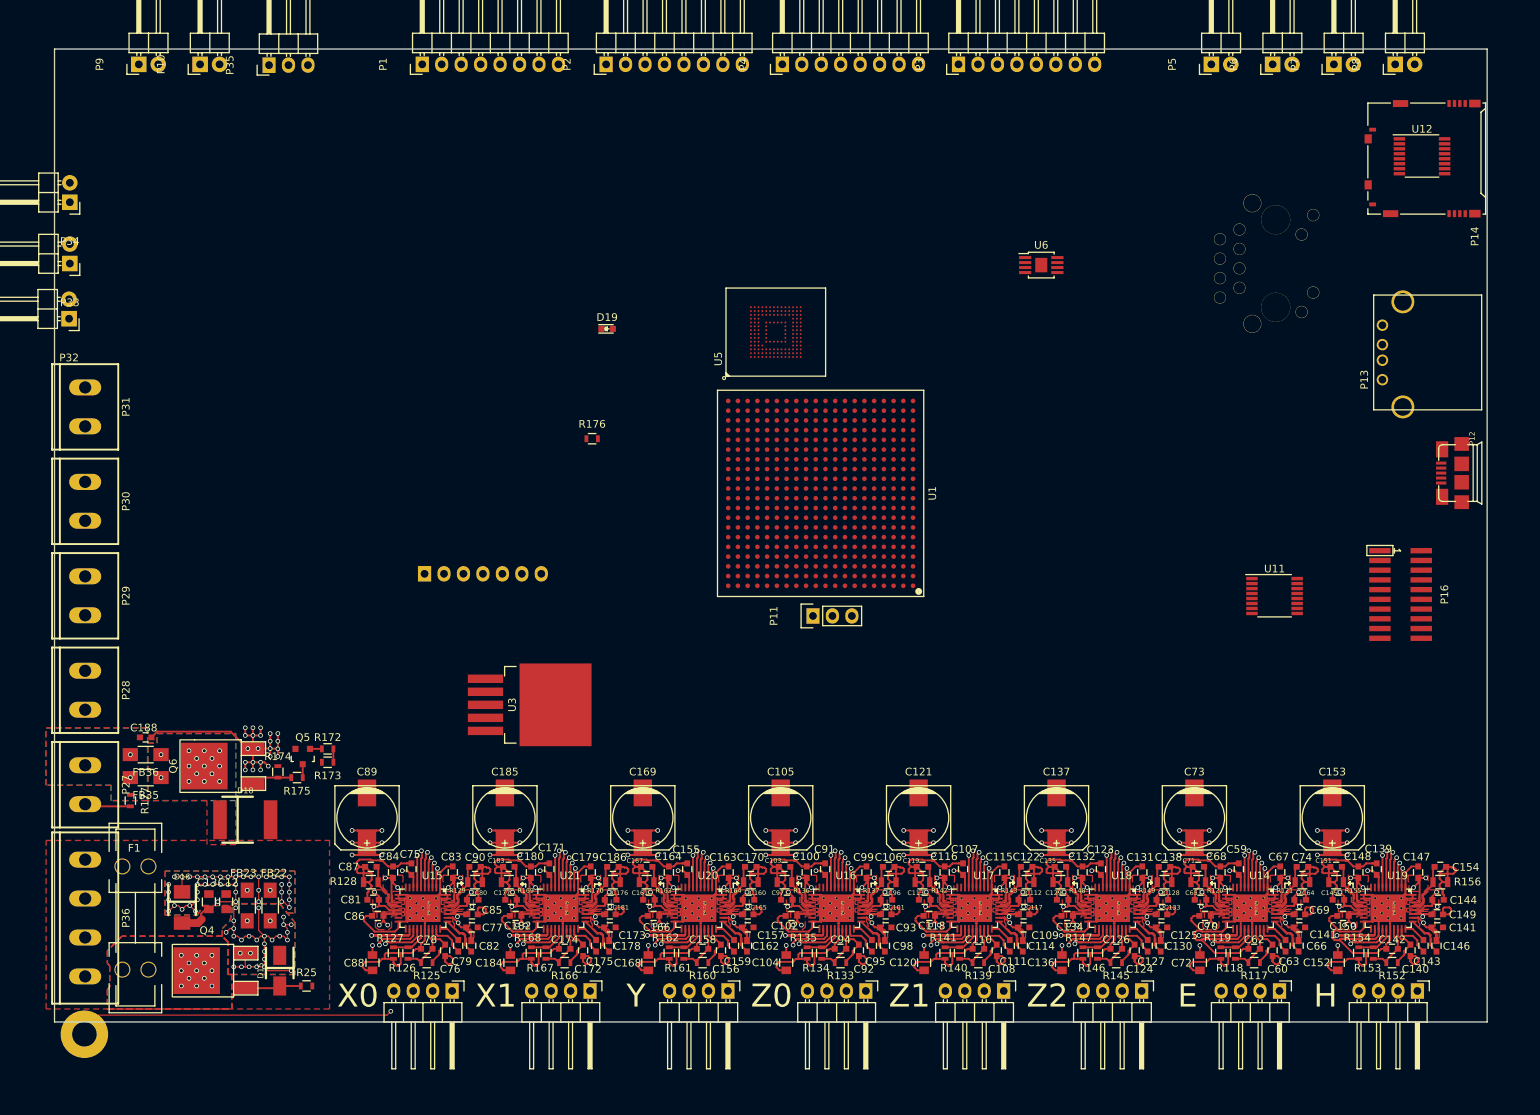
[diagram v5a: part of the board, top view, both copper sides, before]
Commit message: Expose the pad under the tmc2130 stepper drivers
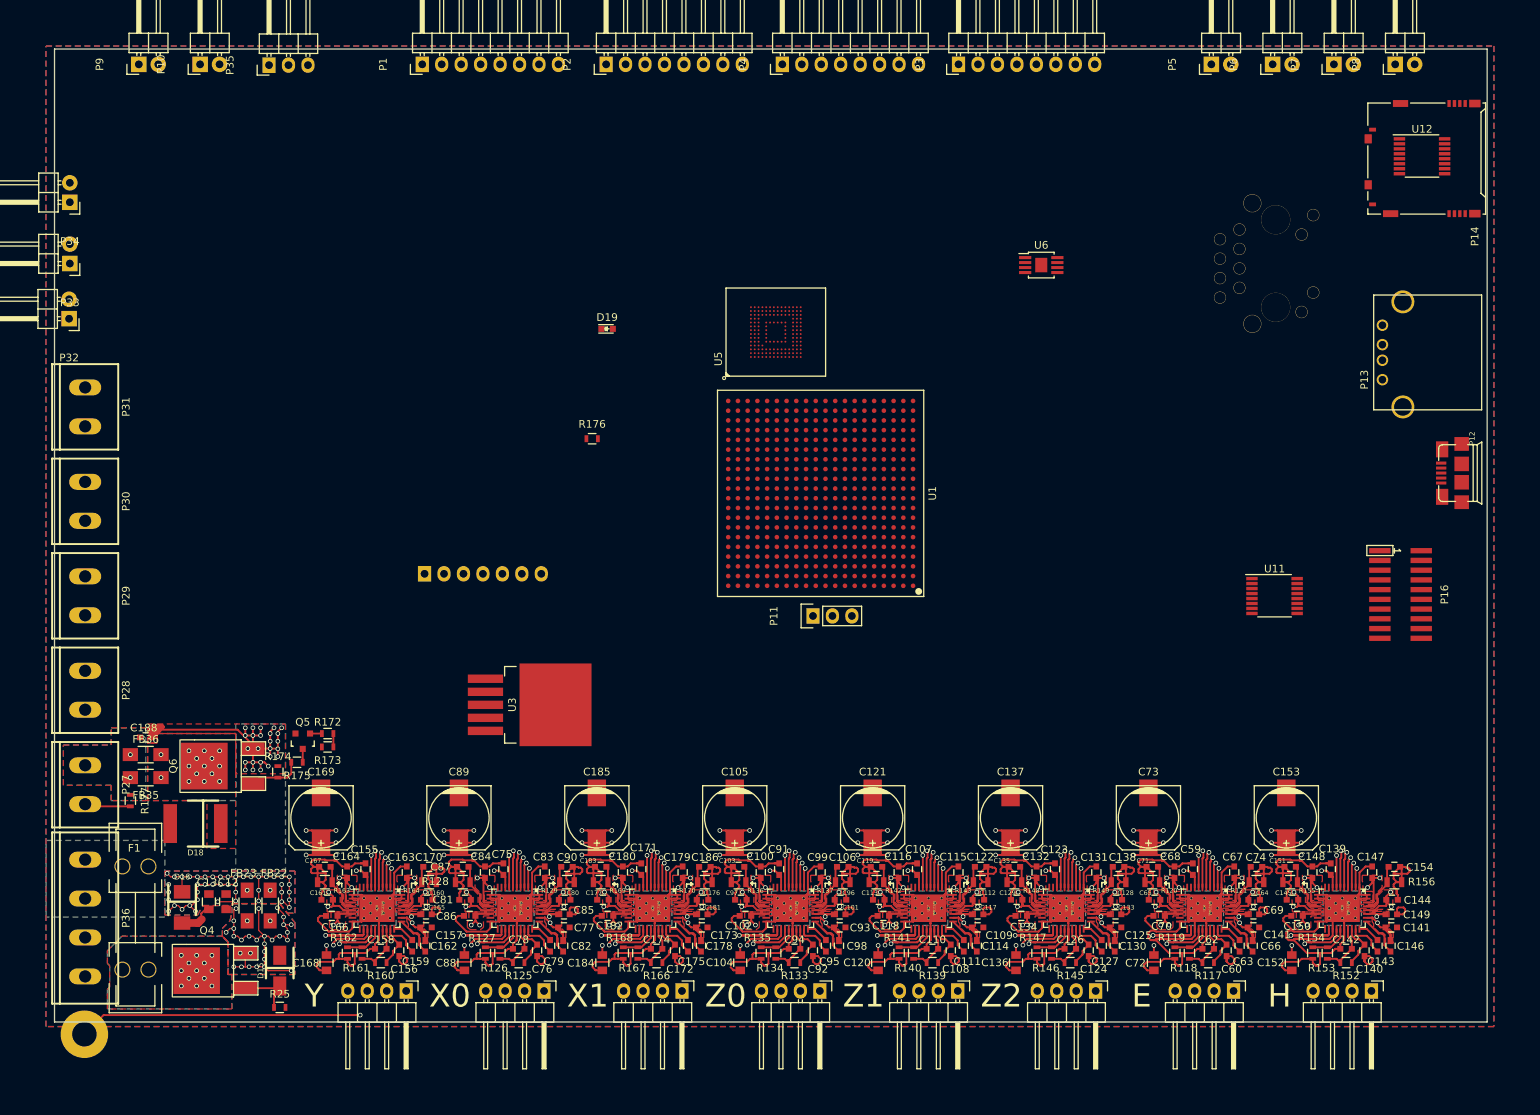
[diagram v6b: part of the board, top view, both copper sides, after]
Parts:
- moved C162 42.0 mm to (110.5, 152.4)
- moved C170 42.0 mm to (111.0, 142.2)
- moved R161 42.0 mm to (102.2, 153.4)
- moved R164 42.0 mm to (111.0, 144.2)
- moved C155 42.0 mm to (102.7, 142.4)
- moved C156 42.0 mm to (107.1, 153.1)
- moved C157 42.0 mm to (110.6, 150.1)
- moved C158 42.0 mm to (104.7, 152.8)
- moved C160 42.0 mm to (110.7, 146.4)
- moved C161 42.0 mm to (97.7, 146.4)
- moved C163 42.0 mm to (108.1, 142.8)
- moved C165 42.0 mm to (110.6, 148.3)
- moved C168 42.0 mm to (97.6, 154.7)
- moved P22 42.0 mm to (108.0, 158.3)
- moved R160 42.0 mm to (104.7, 154.7)
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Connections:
- REF** pad : (no net) -> CGND
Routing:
- net (no net): track 38.5 -> 0.00 mm, vias 1 -> 0
- net CGND: track 903.6 -> 940.6 mm, vias 0 -> 1
- net +24V: track 343.6 -> 349.7 mm, vias 157 -> 160
- net Net-(Q6-Pad1): track 5.33 -> 7.03 mm
- net Net-(D15-Pad1): track 36.5 -> 38.0 mm, vias 30 -> 31
- net /Stepper Drivers/Z0_A2: vias 2 -> 3
- added copper zone on B.Cu, net CGND
- added copper zone on In2.Cu, net CGND
- added copper zone on In3.Cu, net CGND
- added copper zone on B.Cu, net Net-(F1-Pad1)
- added copper zone on In3.Cu, net Net-(F1-Pad1)
